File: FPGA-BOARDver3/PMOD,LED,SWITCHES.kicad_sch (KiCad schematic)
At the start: 86 parts, among them P1 PMOD-Device-x2-Type-Generic-A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, P2 PMOD-Device-x2-Type-Generic-A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, Q1 BC107, Q2 BC107, Q3 BC107, Q4 BC107, Q5 BC107, Q6 BC107, SW2 SW_Push, SW3 SW_Push, SW4 SW_Push, SW5 SW_Push, SW6 SW_SP3T, SW7 SW_SP3T

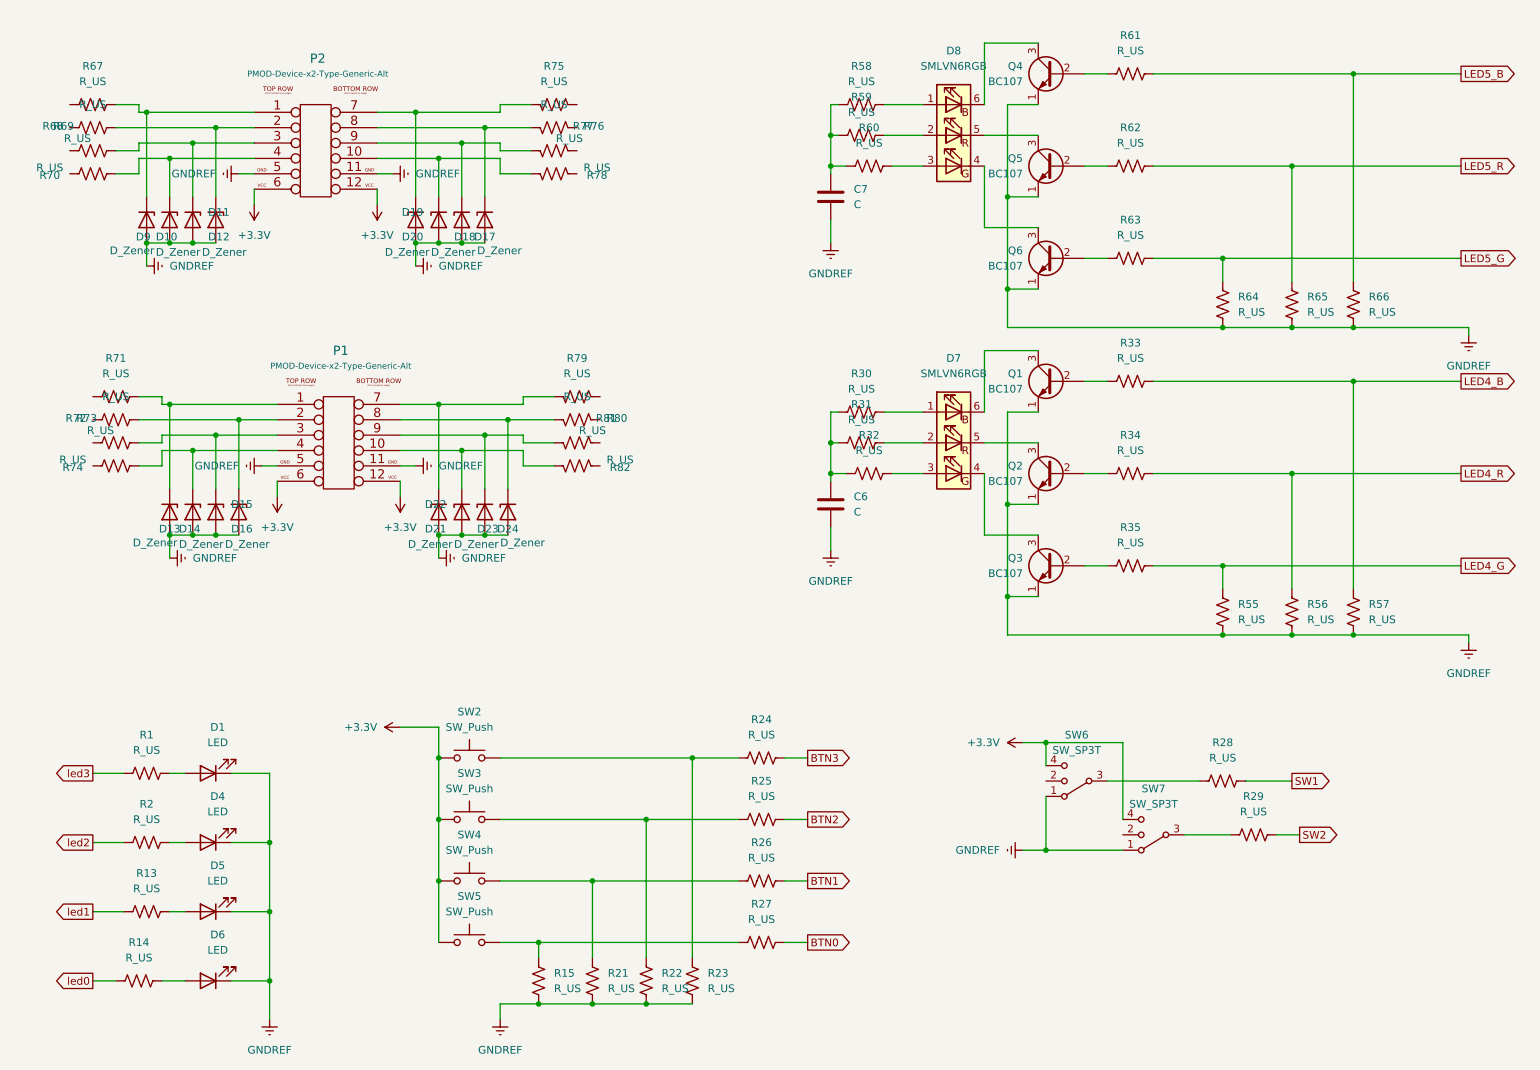
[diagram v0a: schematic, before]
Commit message: power regulation schematic added
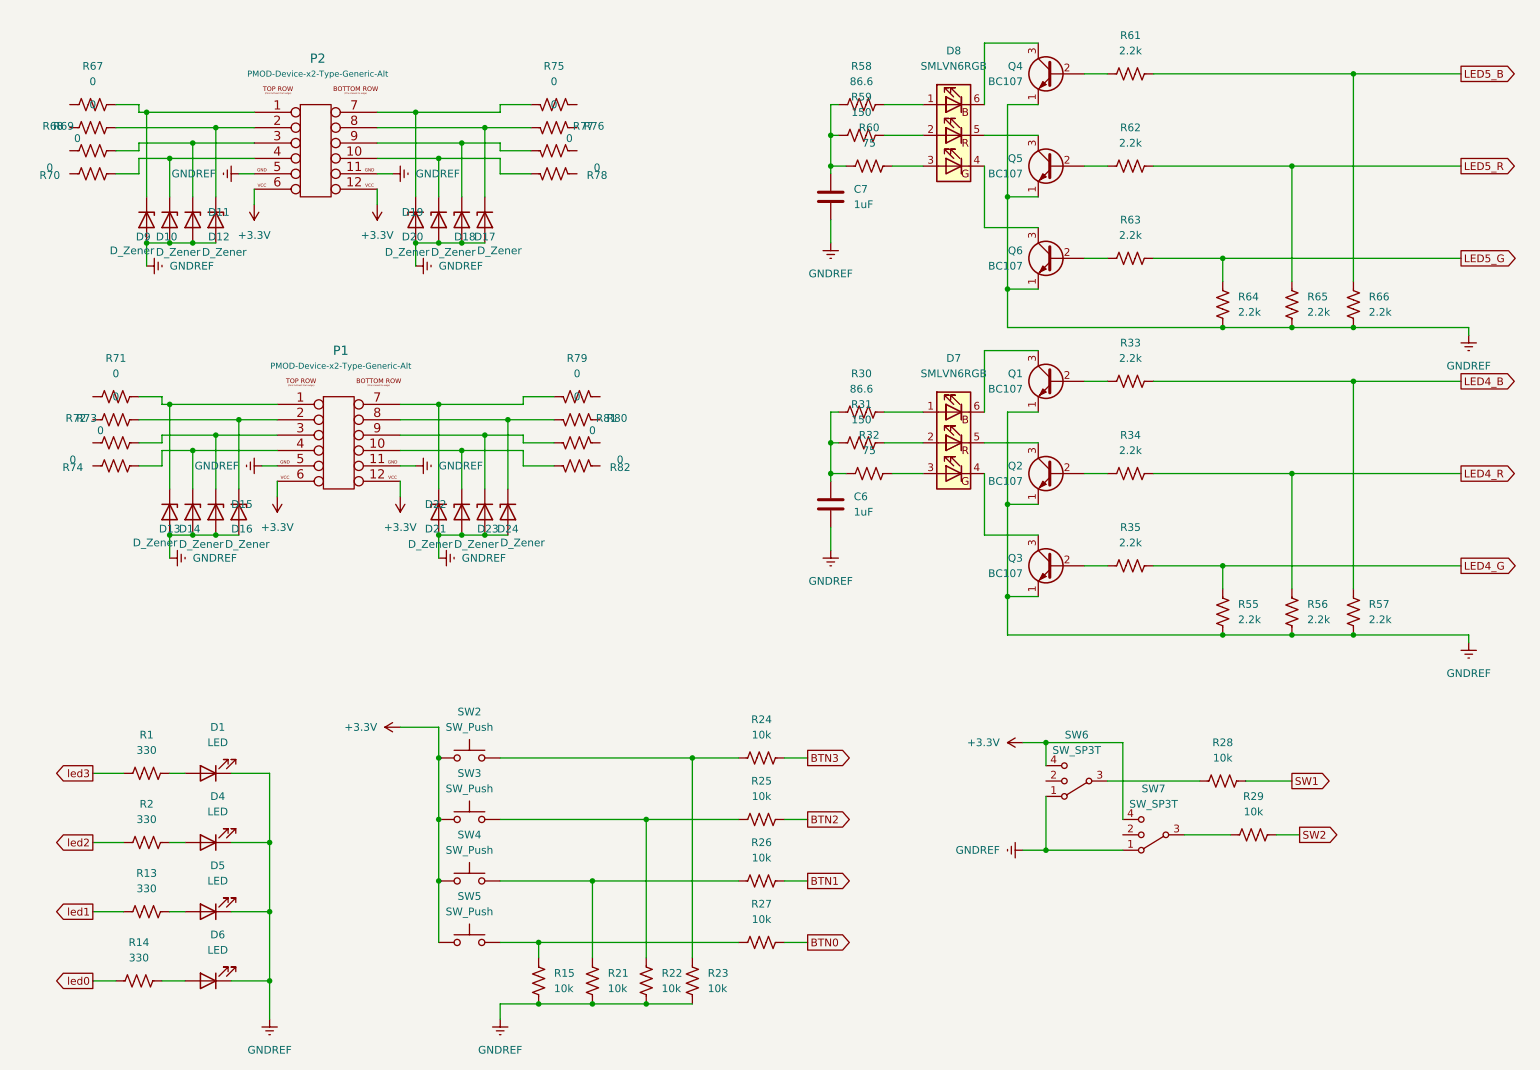
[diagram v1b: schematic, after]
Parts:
- C6, C7: value C -> 1uF
- R1, R13, R14, R2: value R_US -> 330
- R15, R21, R22, R23, R24, R25, R26, R27, R28, R29: value R_US -> 10k
- R30, R58: value R_US -> 86.6
- R31, R59: value R_US -> 150
- R32, R60: value R_US -> 75
- R33, R34, R35, R55, R56, R57, R61, R62, R63, R64, R65, R66: value R_US -> 2.2k
- R67, R68, R69, R70, R71, R72, R73, R74, R75, R76, R77, R78, R79, R80, R81, R82: value R_US -> 0
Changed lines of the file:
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@@
 			)
 		)
-		(property "Value" "R_US"
+		(property "Value" "10k"
 			(at 139.7 160.02 90)
 			(effects
@@
 			)
 		)
-		(property "Value" "R_US"
+		(property "Value" "0"
 			(at 107.95 30.988 90)
 			(effects
@@
 			)
 		)
-		(property "Value" "R_US"
+		(property "Value" "2.2k"
 			(at 218.44 59.6899 0)
 			(effects
@@
 			)
 		)
-		(property "Value" "R_US"
+		(property "Value" "86.6"
 			(at 156.21 21.59 90)
 			(effects
@@
 			)
 		)
-		(property "Value" "R_US"
+		(property "Value" "2.2k"
 			(at 218.44 110.4899 0)
 			(effects
@@
 			)
 		)
-		(property "Value" "R_US"
+		(property "Value" "330"
 			(at 38.1 154.94 90)
 			(effects
@@
 			)
 		)
-		(property "Value" "R_US"
+		(property "Value" "0"
 			(at 112.522 35.814 90)
 			(effects
@@
 			)
 		)
-		(property "Value" "C"
+		(property "Value" "1uF"
 			(at 154.94 41.9099 0)
 			(effects
@@
 			)
 		)
-		(property "Value" "R_US"
+		(property "Value" "0"
 			(at 105.41 25.4 90)
 			(effects
@@
 			)
 		)
-		(property "Value" "R_US"
+		(property "Value" "0"
 			(at 29.21 21.59 90)
 			(effects
@@
 			)
 		)
-		(property "Value" "R_US"
+		(property "Value" "2.2k"
 			(at 240.03 59.6899 0)
 			(effects
@@
 			)
 		)
-		(property "Value" "R_US"
+		(property "Value" "150"
 			(at 156.21 77.47 90)
 			(effects
@@
 			)
 		)
-		(property "Value" "R_US"
+		(property "Value" "2.2k"
 			(at 200.66 82.55 90)
 			(effects
@@
 			)
 		)
-		(property "Value" "R_US"
+		(property "Value" "2.2k"
 			(at 200.66 16.51 90)
 			(effects
@@
 			)
 		)
-		(property "Value" "R_US"
+		(property "Value" "0"
 			(at 33.02 69.85 90)
 			(effects
@@
 			)
 		)
-		(property "Value" "R_US"
+		(property "Value" "10k"
 			(at 123.19 171.4499 0)
 			(effects
@@
 			)
 		)
-		(property "Value" "R_US"
+		(property "Value" "75"
 			(at 157.48 31.75 90)
 			(effects
@@
 			)
 		)
-		(property "Value" "R_US"
+		(property "Value" "10k"
 			(at 139.7 139.7 90)
 			(effects
@@
 			)
 		)
-		(property "Value" "R_US"
+		(property "Value" "2.2k"
 			(at 200.66 67.31 90)
 			(effects
@@
 			)
 		)
-		(property "Value" "R_US"
+		(property "Value" "0"
 			(at 26.67 30.988 90)
 			(effects
@@
 			)
 		)
-		(property "Value" "R_US"
+		(property "Value" "10k"
 			(at 139.7 149.86 90)
 			(effects
@@
 			)
 		)
-		(property "Value" "R_US"
+		(property "Value" "330"
 			(at 38.1 143.51 90)
 			(effects
@@
 			)
 		)
-		(property "Value" "R_US"
+		(property "Value" "10k"
 			(at 220.98 142.24 90)
 			(effects
@@
 			)
 		)
-		(property "Value" "R_US"
+		(property "Value" "330"
 			(at 36.83 166.37 90)
 			(effects
@@
 			)
 		)
-		(property "Value" "R_US"
+		(property "Value" "0"
 			(at 22.098 35.814 90)
 			(effects
@@
 			)
 		)
-		(property "Value" "R_US"
+		(property "Value" "0"
 			(at 30.48 79.248 90)
 			(effects
@@
 			)
 		)
-		(property "Value" "R_US"
+		(property "Value" "0"
 			(at 116.332 84.074 90)
 			(effects
@@
 			)
 		)
-		(property "Value" "R_US"
+		(property "Value" "2.2k"
 			(at 200.66 46.99 90)
 			(effects
@@
 			)
 		)
-		(property "Value" "R_US"
+		(property "Value" "10k"
 			(at 105.41 171.4499 0)
 			(effects
@@
 			)
 		)
-		(property "Value" "R_US"
+		(property "Value" "86.6"
 			(at 156.21 72.39 90)
 			(effects
@@
 			)
 		)
-		(property "Value" "R_US"
+		(property "Value" "2.2k"
 			(at 200.66 31.75 90)
 			(effects
@@
 			)
 		)
-		(property "Value" "C"
+		(property "Value" "1uF"
 			(at 154.94 92.7099 0)
 			(effects
@@
 			)
 		)
-		(property "Value" "R_US"
+		(property "Value" "0"
 			(at 109.22 69.85 90)
 			(effects
@@
 			)
 		)
-		(property "Value" "R_US"
+		(property "Value" "0"
 			(at 111.76 79.248 90)
 			(effects
@@
 			)
 		)
-		(property "Value" "R_US"
+		(property "Value" "0"
 			(at 33.02 73.66 90)
 			(effects
@@
 			)
 		)
-		(property "Value" "R_US"
+		(property "Value" "10k"
 			(at 215.9 133.35 90)
 			(effects
@@
 			)
 		)
-		(property "Value" "R_US"
+		(property "Value" "2.2k"
 			(at 240.03 110.4899 0)
 			(effects
@@
 			)
 		)
-		(property "Value" "R_US"
+		(property "Value" "0"
 			(at 25.908 84.074 90)
 			(effects
@@
 			)
 		)
-		(property "Value" "R_US"
+		(property "Value" "150"
 			(at 156.21 26.67 90)
 			(effects
@@
 			)
 		)
-		(property "Value" "R_US"
+		(property "Value" "330"
 			(at 38.1 132.08 90)
 			(effects
@@
 			)
 		)
-		(property "Value" "R_US"
+		(property "Value" "10k"
 			(at 114.3 171.4499 0)
 			(effects
@@
 			)
 		)
-		(property "Value" "R_US"
+		(property "Value" "10k"
 			(at 130.81 171.4499 0)
 			(effects
@@
 			)
 		)
-		(property "Value" "R_US"
+		(property "Value" "0"
 			(at 105.41 21.59 90)
 			(effects
@@
 			)
 		)
-		(property "Value" "R_US"
+		(property "Value" "2.2k"
 			(at 200.66 97.79 90)
 			(effects
@@
 			)
 		)
-		(property "Value" "R_US"
+		(property "Value" "0"
 			(at 109.22 73.66 90)
 			(effects
@@
 			)
 		)
-		(property "Value" "R_US"
+		(property "Value" "2.2k"
 			(at 229.87 110.4899 0)
 			(effects
@@
 			)
 		)
-		(property "Value" "R_US"
+		(property "Value" "10k"
 			(at 139.7 129.54 90)
 			(effects
@@
 			)
 		)
-		(property "Value" "R_US"
+		(property "Value" "75"
 			(at 157.48 82.55 90)
 			(effects
@@
 			)
 		)
-		(property "Value" "R_US"
+		(property "Value" "2.2k"
 			(at 229.87 59.6899 0)
 			(effects
@@
 			)
 		)
-		(property "Value" "R_US"
+		(property "Value" "0"
 			(at 29.21 25.4 90)
 			(effects

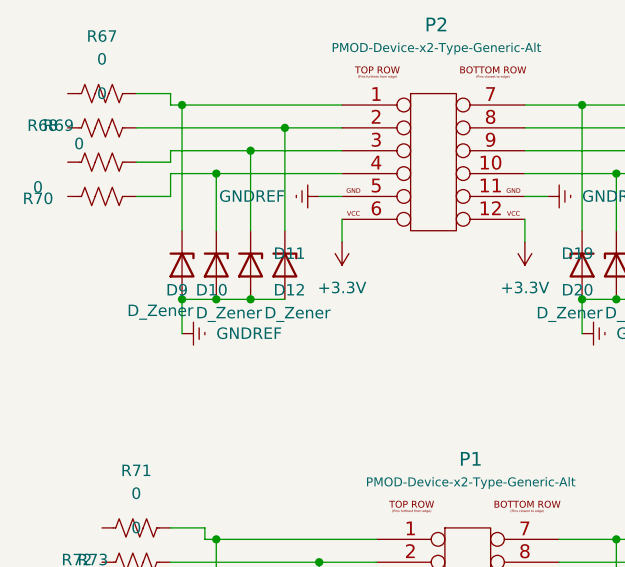
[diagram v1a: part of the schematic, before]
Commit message: assigned footprints for power section and ddr3
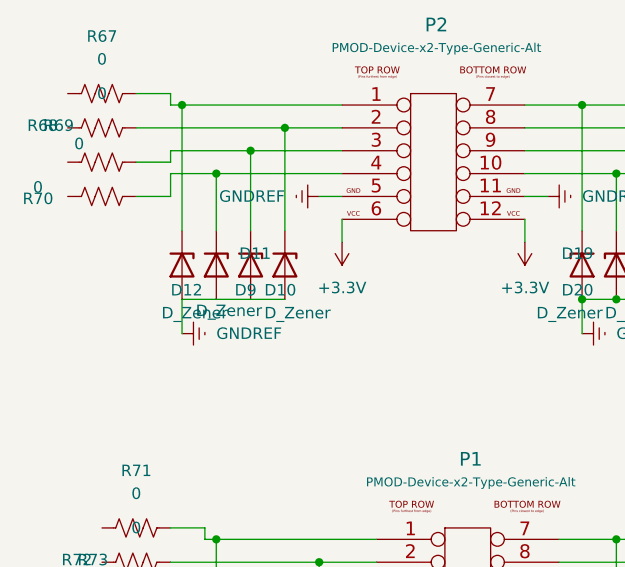
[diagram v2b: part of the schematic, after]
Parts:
- C6, C7: footprint (none) -> JLCPCB:C_0402
- D1, D4, D5, D6: footprint (none) -> LED_SMD:LED_0402_1005Metric
- D10, D11, D12, D13, D14, D15, D16, D17, D18, D19, D20, D21, D22, D23, D24, D9: footprint (none) -> BZT52C5V1_7_F:SOD123_DIO
- D7, D8: footprint LED_SMD:LED_ROHM_SMLVN6 -> SMLVN6RBG1U1:LED_SMLV56_ROM
- R1, R13, R14, R15, R2, R21, R22, R23, R24, R25, R26, R27, R28, R29, R30, R31, R32, R33, R34, R35, R55, R56, R57, R58, R59, R60, R61, R62, R63, R64, R65, R66, R67, R68, R69, R70, R71, R72, R73, R74, R75, R76, R77, R78, R79, R80, R81, R82: footprint (none) -> JLCPCB:R_0402
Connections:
- net GNDREF: no longer D11.2 (A), D9.2 (A)
- net at P2.1 (P1), R67.2: now also D12.1 (K); no longer D9.1 (K)
- net at P2.2 (P2), R68.2: now also D10.1 (K); no longer D12.1 (K)
- net at P2.3 (P3), R69.2: now also D9.1 (K); no longer D11.1 (K)
- net at P2.4 (P4), R70.2: now also D11.1 (K); no longer D10.1 (K)
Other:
- moved on the sheet: D10, D11, D12, D9
